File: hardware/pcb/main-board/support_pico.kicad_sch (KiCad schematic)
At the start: 29 parts, among them J701 Conn_01x02, J702 Z88 SD Card, U702 RP2040, U703 W25Q128JVS, Y701 ABLS-12.000MHZ-B4-T

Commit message: a few more tidyups, almost ready for dual shifts stuff now
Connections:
- net RP2040_PWR renamed RP2040_3V3_PWR
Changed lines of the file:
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@@
 		)
 	)
-	(global_label "RP2040_PWR"
+	(global_label "RP2040_3V3_PWR"
 		(shape input)
 		(at 78.74 20.32 180)
@@
 		)
 	)
-	(global_label "RP2040_PWR"
+	(global_label "RP2040_3V3_PWR"
 		(shape input)
 		(at 200.66 38.1 180)
@@
 		)
 	)
-	(global_label "RP2040_PWR"
+	(global_label "RP2040_3V3_PWR"
 		(shape input)
 		(at 231.14 81.28 180)

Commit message: more support rp2040 cleanups
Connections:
- net RX_FROM_SUPPORT_PICO renamed RX_FROM_SP_RP
- net TX_TO_SUPPORT_PICO renamed TX_TO_SP_RP
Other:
- note added: "SD card for Z88 file system, cartridge images, etc. Also for the application board Pico's note taking apps (etc.) CM4 accesses this via the support RP2040."
- note added: "The design is that the CM4 is the I2C bus master. The Support RP2040 will only be bus master when the I2C is off, and since the Support RP2040 turns on the CM4 it's safe to set them both up as bus masters. They can't clash, even if the I2C drivers don't support multi master."
- note added: "The keyboard RP2040 is always needed when this one is on, so the two RP2040s will use the same power source. This RP2040 will be programmed with knowledge about the side displays (whether they exist, for a start). If the side displays PCB is connected, this RP2040 will send the signal to start it up."
- note removed: "SD card for Z88 file system, cartridge images, etc. Also for the instant-on mode, on the support Pico's note taking apps (etc.) CM4 accesses this via the support Pico."
- note removed: "The design is that the CM4 is the I2C bus master. The Support Pico will only be bus master when the I2C is off, and since the Support Pico turns on the CM4 it's safe to set them both up as bus masters. They can't clash, even if the I2C drivers don't support multi master."
- note removed: "The keyboard Pico is always needed when this one is on, so the two Picos will use the same power source. This Pico will be programmed with knowledge about the side displays (whether they exist, for a start). If the side displays PCB is connected, this Pico will send the signal to start it up."
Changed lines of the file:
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@@
 		)
 	)
-	(text "SD card for Z88 file system, cartridge images, etc.\nAlso for the instant-on mode, on the support Pico's\nnote taking apps (etc.)\n\nCM4 accesses this via the support Pico."
+	(text "SD card for Z88 file system, cartridge images, etc.\nAlso for the application board Pico's note taking\napps (etc.)\n\nCM4 accesses this via the support RP2040."
 		(exclude_from_sim no)
 		(at 180.34 22.86 0)
@@
 		)
 	)
-	(text "The design is that the CM4 is the I2C bus master. The\nSupport Pico will only be bus master when the I2C is\noff, and since the Support Pico turns on the CM4 it's\nsafe to set them both up as bus masters. They can't\nclash, even if the I2C drivers don't support multi master."
+	(text "The design is that the CM4 is the I2C bus master. The\nSupport RP2040 will only be bus master when the I2C is\noff, and since the Support RP2040 turns on the CM4 it's\nsafe to set them both up as bus masters. They can't\nclash, even if the I2C drivers don't support multi master."
 		(exclude_from_sim no)
 		(at 13.97 186.69 0)
@@
 		)
 	)
-	(text "The keyboard Pico is always needed when this one is on,\nso the two Picos will use the same power source.\n\nThis Pico will be programmed with knowledge about the side\ndisplays (whether they exist, for a start). If the side displays\nPCB is connected, this Pico will send the signal to start it up."
+	(text "The keyboard RP2040 is always needed when this one is on,\nso the two RP2040s will use the same power source.\n\nThis RP2040 will be programmed with knowledge about the side\ndisplays (whether they exist, for a start). If the side displays\nPCB is connected, this RP2040 will send the signal to start it up."
 		(exclude_from_sim no)
 		(at 13.97 172.72 0)
@@
 		)
 	)
-	(global_label "TX_TO_SUPPORT_PICO"
+	(global_label "TX_TO_SP_RP"
 		(shape input)
 		(at 160.02 170.18 180)
@@
 		)
 		(property "Intersheetrefs" "${INTERSHEET_REFS}"
-			(at 137.1876 170.18 0)
+			(at 145.2915 170.18 0)
 			(effects
 				(font
@@
 		)
 	)
-	(global_label "RX_FROM_SUPPORT_PICO"
+	(global_label "RX_FROM_SP_RP"
 		(shape input)
 		(at 160.02 177.8 180)
@@
 		)
 		(property "Intersheetrefs" "${INTERSHEET_REFS}"
-			(at 134.0428 177.8 0)
-			(effects
-				(font
-					(size 1.27 1.27)
-				)
-				(justify right)
-				(hide yes)
-			)
-		)
-	)
-	(global_label "RX_FROM_SUPPORT_PICO"
+			(at 142.1467 177.8 0)
+			(effects
+				(font
+					(size 1.27 1.27)
+				)
+				(justify right)
+				(hide yes)
+			)
+		)
+	)
+	(global_label "RX_FROM_SP_RP"
 		(shape output)
 		(at 113.03 71.12 0)
@@
 		)
 		(property "Intersheetrefs" "${INTERSHEET_REFS}"
-			(at 139.0072 71.12 0)
+			(at 130.9033 71.12 0)
 			(effects
 				(font
@@
 		)
 	)
-	(global_label "TX_TO_SUPPORT_PICO"
+	(global_label "TX_TO_SP_RP"
 		(shape input)
 		(at 113.03 73.66 0)
@@
 		)
 		(property "Intersheetrefs" "${INTERSHEET_REFS}"
-			(at 135.8624 73.66 0)
-			(effects
-				(font
+			(at 127.7585 73.66 0)
+			(effects
+				(font

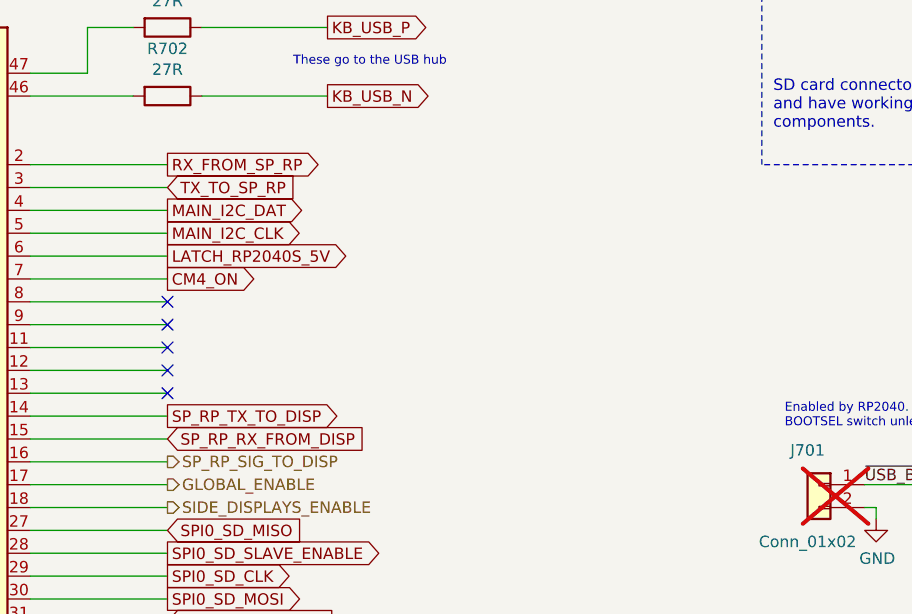
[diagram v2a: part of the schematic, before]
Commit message: update support pico links: UART0 to CM4, UART1 to app board Pico0, GPIOs to app board Pico1. KB pico outstanding
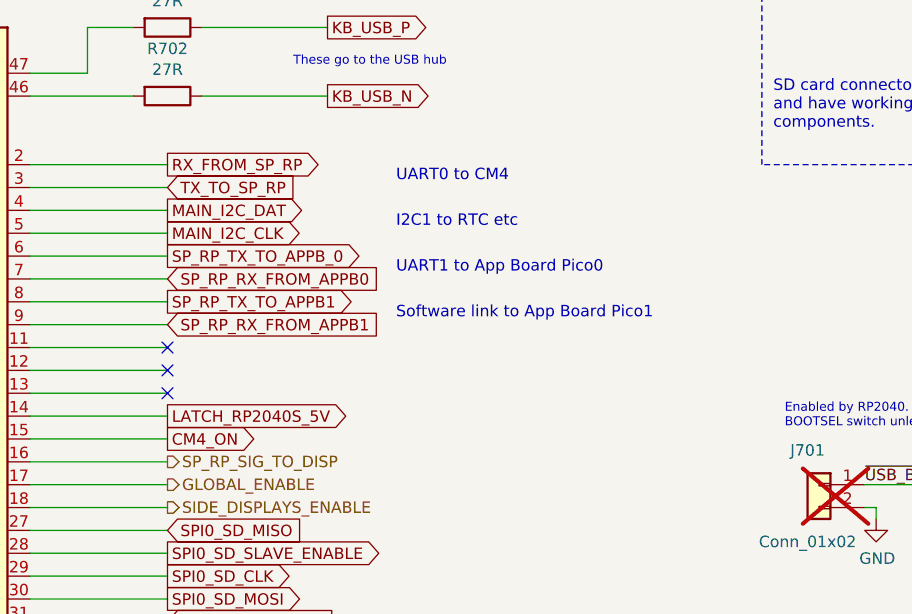
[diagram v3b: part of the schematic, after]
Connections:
- net SP_RP_RX_FROM_DISP is gone; now on net CM4_ON: U702.15 (GPIO12)
- net SP_RP_TX_TO_DISP is gone; now on net LATCH_RP2040S_5V: U702.14 (GPIO11)
- net CM4_ON: no longer U702.7 (GPIO5)
- net LATCH_RP2040S_5V: no longer U702.6 (GPIO4)
- net SP_RP_TX_TO_APPB1: now reaches U702.8 (GPIO6)
- net SP_RP_RX_FROM_APPB1: now reaches U702.9 (GPIO7)
- new net SP_RP_RX_FROM_APPB0: U702.7 (GPIO5)
- new net SP_RP_TX_TO_APPB_0: U702.6 (GPIO4)
- no-connect marks 16 -> 14
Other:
- note added: "I2C1 to RTC etc"
- note added: "Software link to App Board Pico1"
- note added: "UART0 to CM4"
- note added: "UART1 to App Board Pico0"
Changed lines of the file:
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@@
-	)
-	(no_connect
-		(at 113.03 88.9)
 	)
 	(no_connect
@@
 	(no_connect
 		(at 113.03 93.98)
-	)
-	(no_connect
-		(at 113.03 86.36)
 	)
 	(wire
@@
 		)
 	)
+	(text "Software link to App Board Pico1"
+		(exclude_from_sim no)
+		(at 138.43 87.63 0)
+		(effects
+			(font
+				(size 1.27 1.27)
+			)
+			(justify left)
+		)
+	)
 	(text "The design is that the CM4 is the I2C bus master. The\nSupport RP2040 will only be bus master when the I2C is\noff, and since the Support RP2040 turns on the CM4 it's\nsafe to set them both up as bus masters. They can't\nclash, even if the I2C drivers don't support multi master."
 		(exclude_from_sim no)
@@
 		)
 	)
+	(text "UART1 to App Board Pico0"
+		(exclude_from_sim no)
+		(at 138.43 82.55 0)
+		(effects
+			(font
+				(size 1.27 1.27)
+			)
+			(justify left)
+		)
+	)
 	(text "Crystal"
 		(exclude_from_sim no)
@@
 		)
 	)
+	(text "I2C1 to RTC etc"
+		(exclude_from_sim no)
+		(at 138.43 77.47 0)
+		(effects
+			(font
+				(size 1.27 1.27)
+			)
+			(justify left)
+		)
+	)
 	(text "Card detect pin on our components"
 		(exclude_from_sim no)
@@
 		)
 	)
+	(text "UART0 to CM4"
+		(exclude_from_sim no)
+		(at 138.43 72.39 0)
+		(effects
+			(font
+				(size 1.27 1.27)
+			)
+			(justify left)
+		)
+	)
 	(text "Flash, 16MB should be enough\nfor anything this RP2040 might do"
 		(exclude_from_sim no)
@@
 	(global_label "LATCH_RP2040S_5V"
 		(shape output)
-		(at 113.03 81.28 0)
-		(fields_autoplaced yes)
-		(effects
-			(font
-				(size 1.27 1.27)
-			)
-			(justify left)
-		)
-		(property "Intersheetrefs" "${INTERSHEET_REFS}"
-			(at 133.8666 81.28 0)
+		(at 113.03 99.06 0)
+		(fields_autoplaced yes)
+		(effects
+			(font
+				(size 1.27 1.27)
+			)
+			(justify left)
+		)
+		(property "Intersheetrefs" "${INTERSHEET_REFS}"
+			(at 133.8666 99.06 0)
 			(effects
 				(font
@@
 		)
 	)
-	(global_label "SP_RP_TX_TO_DISP"
+	(global_label "SP_RP_TX_TO_APPB_0"
 		(shape output)
-		(at 113.03 99.06 0)
-		(fields_autoplaced yes)
-		(effects
-			(font
-				(size 1.27 1.27)
-			)
-			(justify left)
-		)
-		(property "Intersheetrefs" "${INTERSHEET_REFS}"
-			(at 133.0804 99.06 0)
+		(at 113.03 81.28 0)
+		(fields_autoplaced yes)
+		(effects
+			(font
+				(size 1.27 1.27)
+			)
+			(justify left)
+		)
+		(property "Intersheetrefs" "${INTERSHEET_REFS}"
+			(at 135.8018 81.28 0)
 			(effects
 				(font
@@
 	(global_label "CM4_ON"
 		(shape output)
-		(at 113.03 83.82 0)
-		(fields_autoplaced yes)
-		(effects
-			(font
-				(size 1.27 1.27)
-			)
-			(justify left)
-		)
-		(property "Intersheetrefs" "${INTERSHEET_REFS}"
-			(at 122.9205 83.82 0)
+		(at 113.03 101.6 0)
+		(fields_autoplaced yes)
+		(effects
+			(font
+				(size 1.27 1.27)
+			)
+			(justify left)
+		)
+		(property "Intersheetrefs" "${INTERSHEET_REFS}"
+			(at 122.9205 101.6 0)
 			(effects
 				(font
@@
 		)
 	)
+	(global_label "SP_RP_TX_TO_APPB1"
+		(shape output)
+		(at 113.03 86.36 0)
+		(fields_autoplaced yes)
+		(effects
+			(font
+				(size 1.27 1.27)
+			)
+			(justify left)
+		)
+		(property "Intersheetrefs" "${INTERSHEET_REFS}"
+			(at 134.8342 86.36 0)
+			(effects
+				(font
+					(size 1.27 1.27)
+				)
+				(justify left)
+				(hide yes)
+			)
+		)
+	)
 	(global_label "SD_CARD_DETECT"
 		(shape input)
@@
 		)
 	)
-	(global_label "SP_RP_RX_FROM_DISP"
+	(global_label "SP_RP_RX_FROM_APPB0"
 		(shape input)
-		(at 113.03 101.6 0)
-		(fields_autoplaced yes)
-		(effects
-			(font
-				(size 1.27 1.27)
-			)
-			(justify left)
-		)
-		(property "Intersheetrefs" "${INTERSHEET_REFS}"
-			(at 136.2252 101.6 0)
-			(effects
-				(font
+		(at 113.03 83.82 0)
+		(fields_autoplaced yes)
+		(effects
+			(font
+				(size 1.27 1.27)
+			)
+			(justify left)
+		)
+		(property "Intersheetrefs" "${INTERSHEET_REFS}"
+			(at 137.979 83.82 0)
+			(effects
+				(font
+					(size 1.27 1.27)
+				)
+				(justify left)
+				(hide yes)
+			)
+		)
+	)
+	(global_label "SP_RP_RX_FROM_APPB1"
+		(shape input)
+		(at 113.03 88.9 0)
+		(fields_autoplaced yes)
+		(effects
+			(font
+				(size 1.27 1.27)
+			)
+			(justify left)
+		)
+		(property "Intersheetrefs" "${INTERSHEET_REFS}"
+			(at 137.979 88.9 0)
+			(effects
+				(font

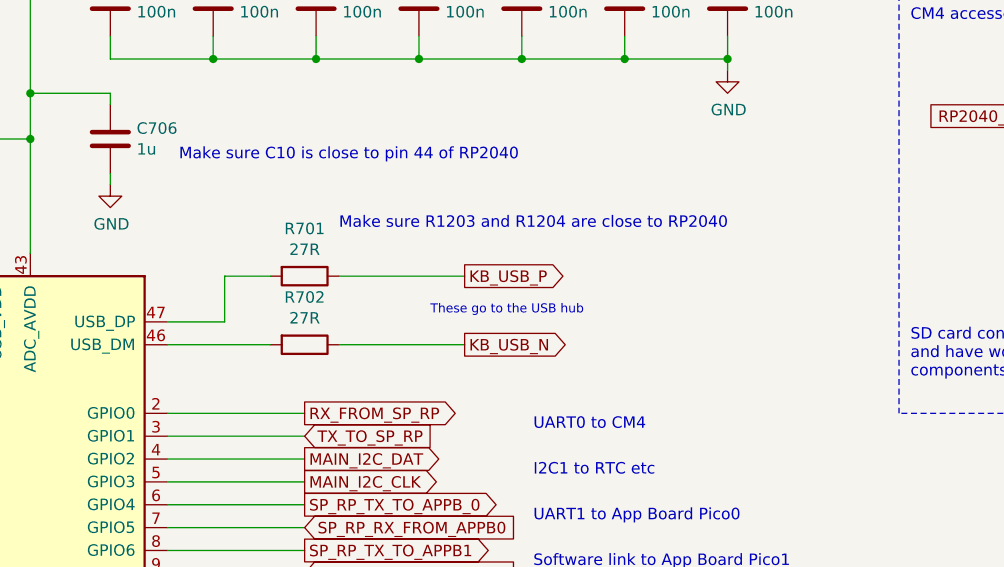
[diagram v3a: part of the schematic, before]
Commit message: disconnect the keyboard pico from the support pico, that link isn't required
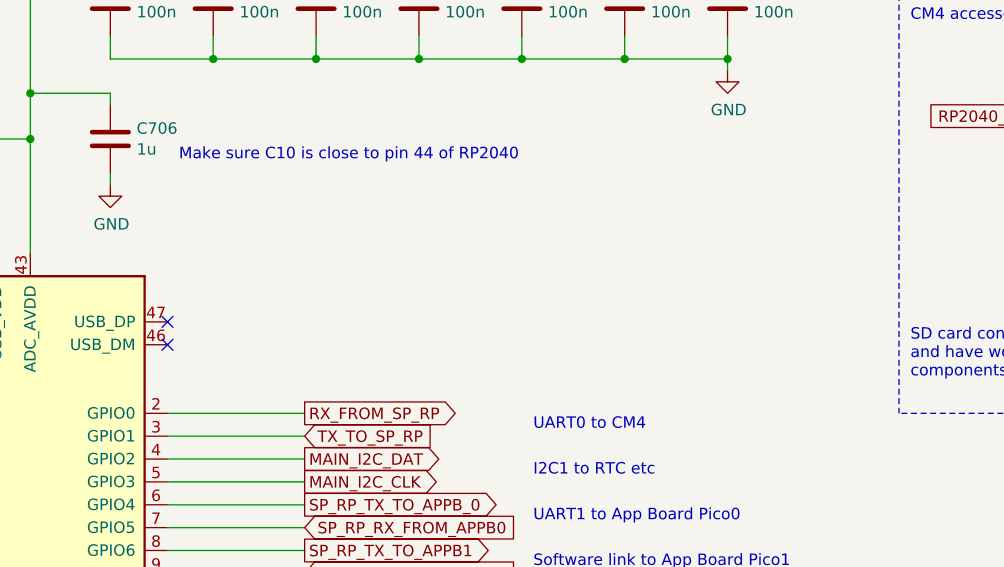
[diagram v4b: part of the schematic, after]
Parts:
- removed R701, R702: 27R, Capacitor_SMD:C_0402_1005Metric, symbol Device:R
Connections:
- no-connect marks 14 -> 16
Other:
- note removed: "Make sure R1203 and R1204 are close to RP2040"
- note removed: "These go to the USB hub"

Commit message: rename display board things to application board things
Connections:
- net SIDE_DISPLAYS_ENABLE renamed APP_BOARD_ENABLE
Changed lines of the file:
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@@
 		)
 	)
-	(hierarchical_label "SIDE_DISPLAYS_ENABLE"
+	(hierarchical_label "APP_BOARD_ENABLE"
 		(shape output)
 		(at 113.03 109.22 0)
@@
 		)
 	)
-	(hierarchical_label "SIDE_DISPLAYS_ENABLE"
+	(hierarchical_label "APP_BOARD_ENABLE"
 		(shape input)
 		(at 160.02 194.31 180)

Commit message: more renaming and tidying up of internal interfaces
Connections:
- net SP_RP_SIG_TO_DISP renamed SP_RP_SIG_TO_APPB
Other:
- note added: "Binary signal to the application board"
- note added: "Pull high to power up the application board"
- note added: "Pull low to reboot the CM4"
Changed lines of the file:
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@@
+		)
+	)
+	(text "Pull high to power up the application board"
+		(exclude_from_sim no)
+		(at 138.43 109.22 0)
+		(effects
+			(font
+				(size 1.27 1.27)
+			)
+			(justify left)
+		)
+	)
+	(text "Pull low to reboot the CM4"
+		(exclude_from_sim no)
+		(at 138.43 106.68 0)
+		(effects
+			(font
+				(size 1.27 1.27)
+			)
+			(justify left)
+		)
+	)
+	(text "Binary signal to the application board"
+		(exclude_from_sim no)
+		(at 138.43 104.14 0)
+		(effects
+			(font
+				(size 1.27 1.27)
+			)
+			(justify left)
 		)
 	)
@@
 		)
 	)
-	(hierarchical_label "SP_RP_SIG_TO_DISP"
+	(hierarchical_label "SP_RP_SIG_TO_APPB"
 		(shape output)
 		(at 113.03 104.14 0)

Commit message: tidy the keyboard comms
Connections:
- net SP_RP_TX_TO_APPB_0 renamed SP_RP_TX_TO_APPB0
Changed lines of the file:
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@@
 		)
 	)
-	(global_label "SP_RP_TX_TO_APPB_0"
+	(global_label "SP_RP_TX_TO_APPB0"
 		(shape output)
 		(at 113.03 81.28 0)
@@
 		)
 		(property "Intersheetrefs" "${INTERSHEET_REFS}"
-			(at 135.8018 81.28 0)
+			(at 134.8342 81.28 0)
 			(effects
 				(font

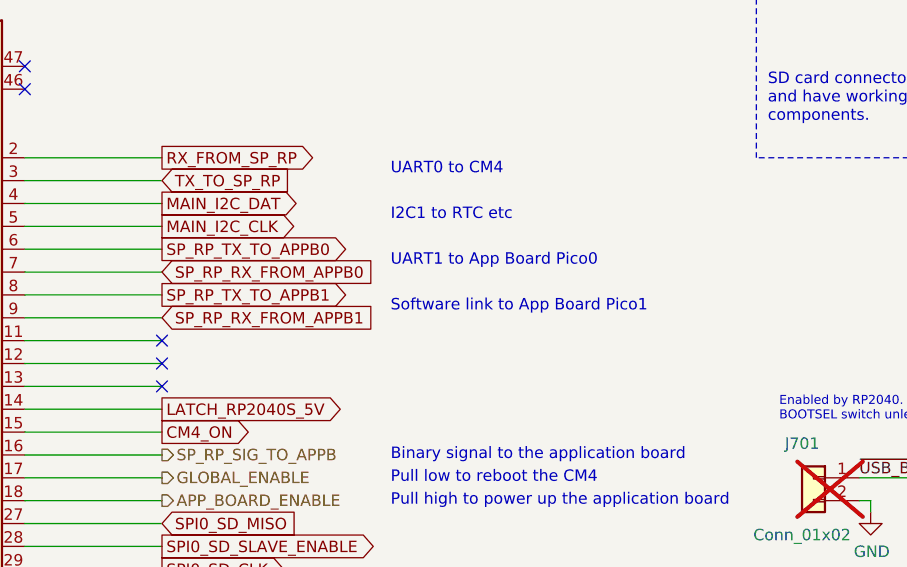
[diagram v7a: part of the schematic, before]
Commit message: rename app board picos to 1 and 2, to match the application board schematics
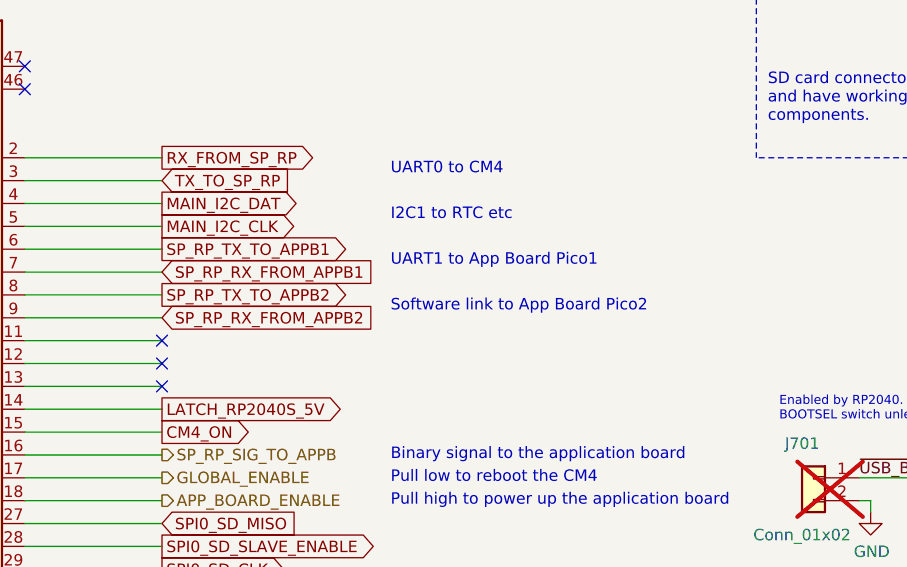
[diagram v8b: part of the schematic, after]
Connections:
- net SP_RP_RX_FROM_APPB0 is gone; now on net SP_RP_RX_FROM_APPB1: U702.7 (GPIO5)
- net SP_RP_TX_TO_APPB0 is gone; now on net SP_RP_TX_TO_APPB1: U702.6 (GPIO4)
- net SP_RP_RX_FROM_APPB1: no longer U702.9 (GPIO7)
- net SP_RP_TX_TO_APPB1: no longer U702.8 (GPIO6)
- new net SP_RP_RX_FROM_APPB2: U702.9 (GPIO7)
- new net SP_RP_TX_TO_APPB2: U702.8 (GPIO6)
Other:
- note added: "Software link to App Board Pico2"
- note added: "UART1 to App Board Pico1"
- note removed: "Software link to App Board Pico1"
- note removed: "UART1 to App Board Pico0"
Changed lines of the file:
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@@
 		)
 	)
-	(text "Software link to App Board Pico1"
+	(text "Software link to App Board Pico2"
 		(exclude_from_sim no)
 		(at 138.43 87.63 0)
@@
 		)
 	)
-	(text "UART1 to App Board Pico0"
+	(text "UART1 to App Board Pico1"
 		(exclude_from_sim no)
 		(at 138.43 82.55 0)
@@
 		)
 	)
-	(global_label "SP_RP_TX_TO_APPB0"
+	(global_label "SP_RP_TX_TO_APPB1"
 		(shape output)
 		(at 113.03 81.28 0)
@@
 		)
 	)
-	(global_label "SP_RP_TX_TO_APPB1"
+	(global_label "SP_RP_TX_TO_APPB2"
 		(shape output)
 		(at 113.03 86.36 0)
@@
 		)
 	)
-	(global_label "SP_RP_RX_FROM_APPB0"
+	(global_label "SP_RP_RX_FROM_APPB1"
 		(shape input)
 		(at 113.03 83.82 0)
@@
 		)
 	)
-	(global_label "SP_RP_RX_FROM_APPB1"
+	(global_label "SP_RP_RX_FROM_APPB2"
 		(shape input)
 		(at 113.03 88.9 0)
